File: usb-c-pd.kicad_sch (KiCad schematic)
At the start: 52 parts, among them J1 USB_C_Receptacle_USB2.0_14P, J2 Barrel_Jack_Switch, J3 Conn_ARM_SWD_TagConnect_TC203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, Q1 T2N7002AK, U1 CYPD3177-24LQ, U2 STM32C071F8Px, U3 INA180A2, U4 XL1509-3.3

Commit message: feat: routing
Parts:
- J1: footprint Connector_USB:USB_C_Receptacle_Amphenol_12401948E412A -> usb-c-pd-lib:GCT_USB4105-GF-A; symbol Connector:USB_C_Receptacle_USB2.0_16P -> usb-c-pd-prodj-lib:USB4105-GF-A; Check_prices (none) -> https://www.snapeda.com/parts/USB4105-GF-A/Global+Connector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; Description_1 (none) -> USB-C (USB TYPE-C) USB 2.0 Receptacle Connector 24 (16+8 Du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; DigiKey_Part_Number (none) -> 2073-USB4105-GF-ACT-ND; MANUFACTURER (none) -> GCT; MAXIMUM_PACKAGE_HEIGHT (none) -> 3.31 mm; MF (none) -> GCT; MP (none) -> USB4105-GF-A; PARTREV (none) -> B4; Package (none) -> None; STANDARD (none) -> Manufacturer Recommendations; SnapEDA_Link (none) -> https://www.snapeda.com/parts/USB4105-GF-A/Global+Connector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
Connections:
- net +3V3: no longer R1.2, R3.1, R4.1
- net +3V3 MCU: now also R1.2, R3.1, R4.1
- net GND: now also J1.A1_B12 (GND), J1.B1_A12 (GND), J1.SH1 (SHELL_GND), J1.SH2 (SHELL_GND), J1.SH3 (SHELL_GND), J1.SH4 (SHELL_GND); no longer J1.A1 (GND), J1.A12 (GND), J1.B1 (GND), J1.B12 (GND)
- net HPI_INT: now also U2.2 (PC14); no longer U2.3 (PC15)
- net PD_GPIO: now also U2.3 (PC15); no longer U2.2 (PC14)
- net VBUS: now also J1.A4_B9 (VBUS), J1.B4_A9 (VBUS); no longer J1.A4 (VBUS), J1.A9 (VBUS), J1.B4 (VBUS), J1.B9 (VBUS)
- net CC2: now reaches J1.B5 (CC2), U1.14 (CC2)
- net CC1: now reaches J1.A5 (CC1), U1.15 (CC1)
- no-connect marks 8 -> 7
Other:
- moved on the sheet: C16

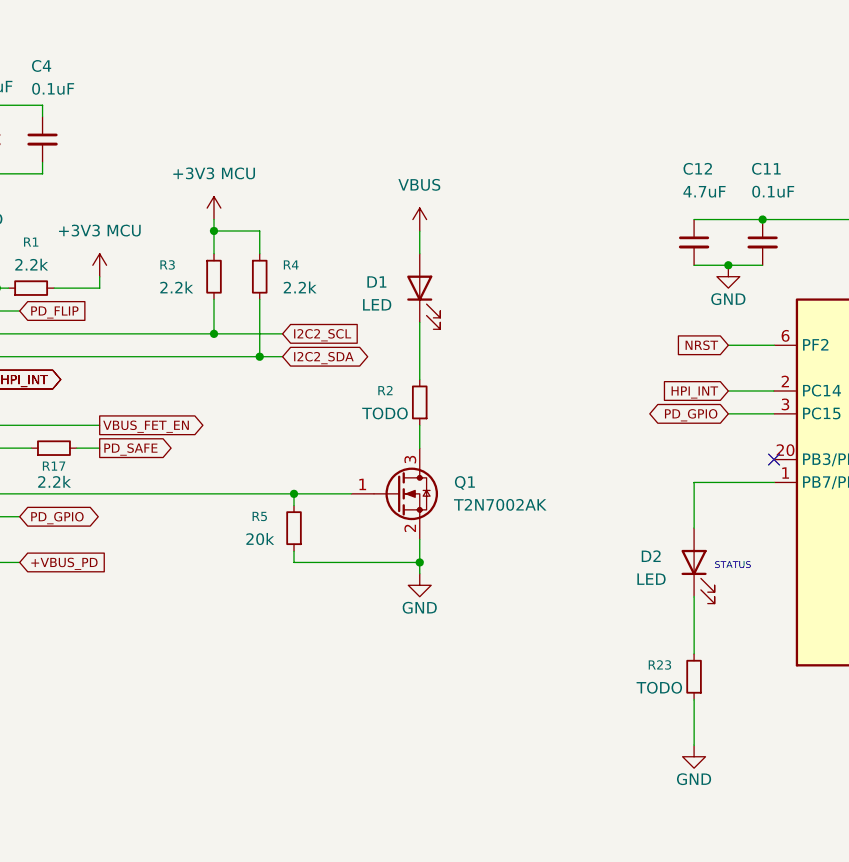
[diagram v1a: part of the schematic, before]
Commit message: feat: add 3d models and diode R values
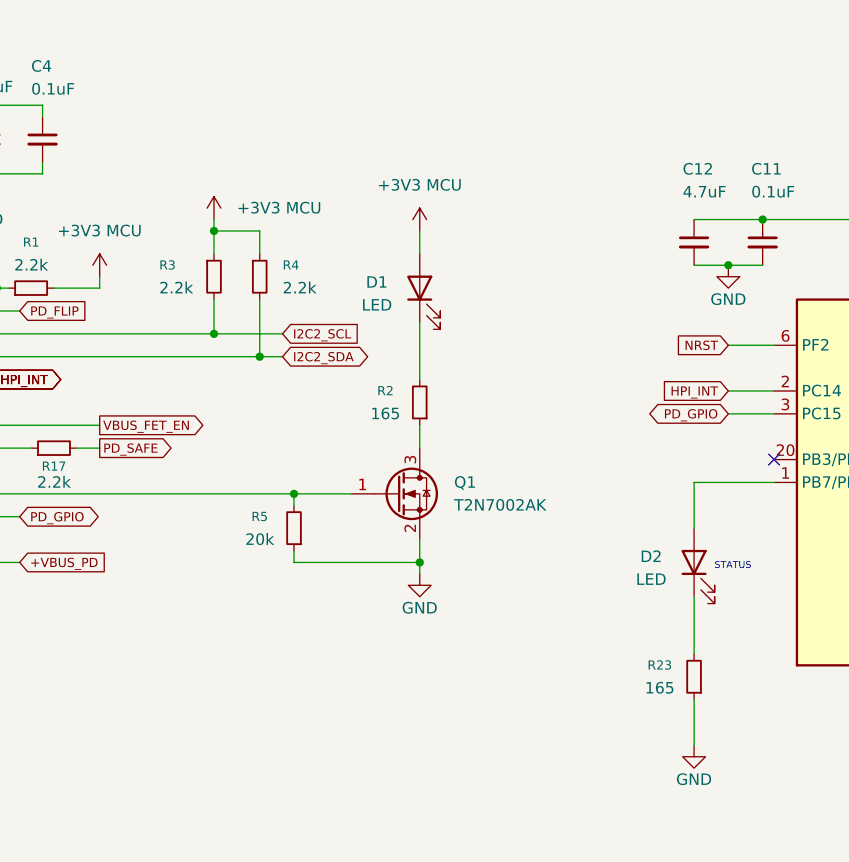
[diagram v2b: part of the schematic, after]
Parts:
- R2, R23: value TODO -> 165
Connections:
- net +3V3 MCU: now also D1.2 (A)
- net VBUS: no longer D1.2 (A)
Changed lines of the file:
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@@
 			)
 		)
-		(property "Value" "VBUS"
+		(property "Value" "+3V3 MCU"
 			(at 186.69 101.6 0)
 			(effects
@@
 			)
 		)
-		(property "Value" "TODO"
+		(property "Value" "165"
 			(at 182.88 127 0)
 			(effects
@@
 		)
 		(property "Value" "+3V3 MCU"
-			(at 163.83 100.33 0)
+			(at 166.37 104.1399 0)
 			(effects
 				(font
 					(size 1.27 1.27)
 				)
+				(justify left)
 			)
 		)
@@
 			)
 		)
-		(property "Value" "TODO"
+		(property "Value" "165"
 			(at 213.36 157.48 0)
 			(effects

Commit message: feat: finalize design
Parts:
- added H1, H2: MountingHole_Pad, MountingHole:MountingHole_3.2mm_M3_DIN965_Pad, symbol Mechanical:MountingHole_Pad
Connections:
- net GND: now also H1.1, H2.1
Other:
- note added: "3V3 Buck-Converter"
- note added: "Barrel jack and current sense amplifier"
- note added: "Power delivery rail from EZ PD (controlled by U1)"
- moved on the sheet: C5, C6, C7, J2, Q2A, Q2B, R14, R15, R16, R18
